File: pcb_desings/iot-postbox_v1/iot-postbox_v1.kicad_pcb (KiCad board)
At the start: 2 copper layers, 59 x 34 mm, 87 parts, among them J1 USB_B_Micro, J3 LED, J4 BAT, J5 3V3_LDO2, J6 EXT1, J7 EXT2, Q1 AO3401A, SW1 SW1, SW2 SW2, U1 ESP32-S2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

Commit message: Added iot-postbox_v1 sch to v1.1. Added minor documentation
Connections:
- net 3V3_LDO2_EN renamed LDO2_EN
- net Net-(R3-Pad1) renamed GPIO18
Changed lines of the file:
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@@
   (net 35 "Net-(JP5-Pad1)")
   (net 36 "VBAT_STAT_SENSE")
-  (net 37 "3V3_LDO2_EN")
+  (net 37 "LDO2_EN")
   (net 38 "Net-(JP6-Pad2)")
   (net 39 "/MCU/SPICS0")
@@
   (net 73 "Net-(R1-Pad1)")
   (net 74 "Net-(R2-Pad1)")
-  (net 75 "Net-(R3-Pad1)")
+  (net 75 "GPIO18")
   (footprint "Resistor_SMD:R_0805_2012Metric" locked (layer "F.Cu")
     (at 151.22 101.77 90)
@@
       (net 32 "RGB_LED_PWM") (pinfunction "GPIO17/ADC2_CH6/DAC_1") (pintype "bidirectional"))
     (pad "24" smd roundrect locked (at 1 3.4375) (size 0.22 0.875) (layers "F.Cu" "F.Paste" "F.Mask") (roundrect_rratio 0.25)
-      (net 75 "Net-(R3-Pad1)") (pinfunction "GPIO18/ADC2_CH7/DAC_2") (pintype "bidirectional"))
+      (net 75 "GPIO18") (pinfunction "GPIO18/ADC2_CH7/DAC_2") (pintype "bidirectional"))
     (pad "25" smd roundrect locked (at 1.4 3.4375) (size 0.22 0.875) (layers "F.Cu" "F.Paste" "F.Mask") (roundrect_rratio 0.25)
       (net 74 "Net-(R2-Pad1)") (pinfunction "GPIO19/ADC2_CH8/USB_D-") (pintype "bidirectional"))
@@
       (net 7 "3V3_LDO") (pinfunction "VDD3P3_RTC_IO") (pintype "power_in"))
     (pad "28" smd roundrect locked (at 2.6 3.4375) (size 0.22 0.875) (layers "F.Cu" "F.Paste" "F.Mask") (roundrect_rratio 0.25)
-      (net 37 "3V3_LDO2_EN") (pinfunction "GPIO21") (pintype "bidirectional"))
+      (net 37 "LDO2_EN") (pinfunction "GPIO21") (pintype "bidirectional"))
     (pad "29" smd roundrect locked (at 3.4375 2.6) (size 0.875 0.22) (layers "F.Cu" "F.Paste" "F.Mask") (roundrect_rratio 0.25)
       (net 40 "/MCU/SPICS1") (pinfunction "SPI_CS1/GPIO26") (pintype "bidirectional"))
@@
     (descr "Resistor SMD 0805 (2012 Metric), square (rectangular) end terminal, IPC_7351 nominal, (Body size source: IPC-SM-782 page 72, https://www.pcb-3d.com/wordpress/wp-content/uploads/ipc-sm-782a_amendment_1_and_2.pdf), generated with kicad-footprint-generator")
     (tags "resistor")
-    (property "Mouser" "RR1220P-202-D")
+    (property "Mouser" "RT0805FRE072KL")
     (property "Sheetfile" "INTERFACE.kicad_sch")
     (property "Sheetname" "INTERFACE")
@@
     (tags "resistor")
     (property "Mouser" "RC0603JR-0710KL")
+    (property "Populated" "TBD")
     (property "Sheetfile" "MCU.kicad_sch")
     (property "Sheetname" "MCU")
@@
     (fp_line (start 0.8 -0.4125) (end 0.8 0.4125) (layer "F.Fab") (width 0.1))
     (pad "1" smd roundrect locked (at -0.825 0 270) (size 0.8 0.95) (layers "F.Cu" "F.Paste" "F.Mask") (roundrect_rratio 0.25)
-      (net 75 "Net-(R3-Pad1)") (pintype "passive"))
+      (net 75 "GPIO18") (pintype "passive"))
     (pad "2" smd roundrect locked (at 0.825 0 270) (size 0.8 0.95) (layers "F.Cu" "F.Paste" "F.Mask") (roundrect_rratio 0.25)
       (net 7 "3V3_LDO") (pintype "passive"))
@@
     (descr "Inductor SMD 0402 (1005 Metric), square (rectangular) end terminal, IPC_7351 nominal, (Body size source: http://www.tortai-tech.com/upload/download/2011102023233369053.pdf), generated with kicad-footprint-generator")
     (tags "inductor")
-    (property "Mouser" "LCCI0402S4N7GTAR")
+    (property "Mouser" "LCCI0402S4N7GTAR or shielded 7447840047G")
     (property "Sheetfile" "MCU.kicad_sch")
     (property "Sheetname" "MCU")
@@
     (fp_line (start -2.3 1.25) (end -2.3 -1.25) (layer "B.CrtYd") (width 0.05))
     (pad "1" smd custom locked (at -1.3 0 270) (size 1 0.5) (layers "B.Cu" "B.Mask")
-      (net 37 "3V3_LDO2_EN") (pinfunction "A") (pintype "passive") (zone_connect 2)
+      (net 37 "LDO2_EN") (pinfunction "A") (pintype "passive") (zone_connect 2)
       (options (clearance outline) (anchor rect))
       (primitives

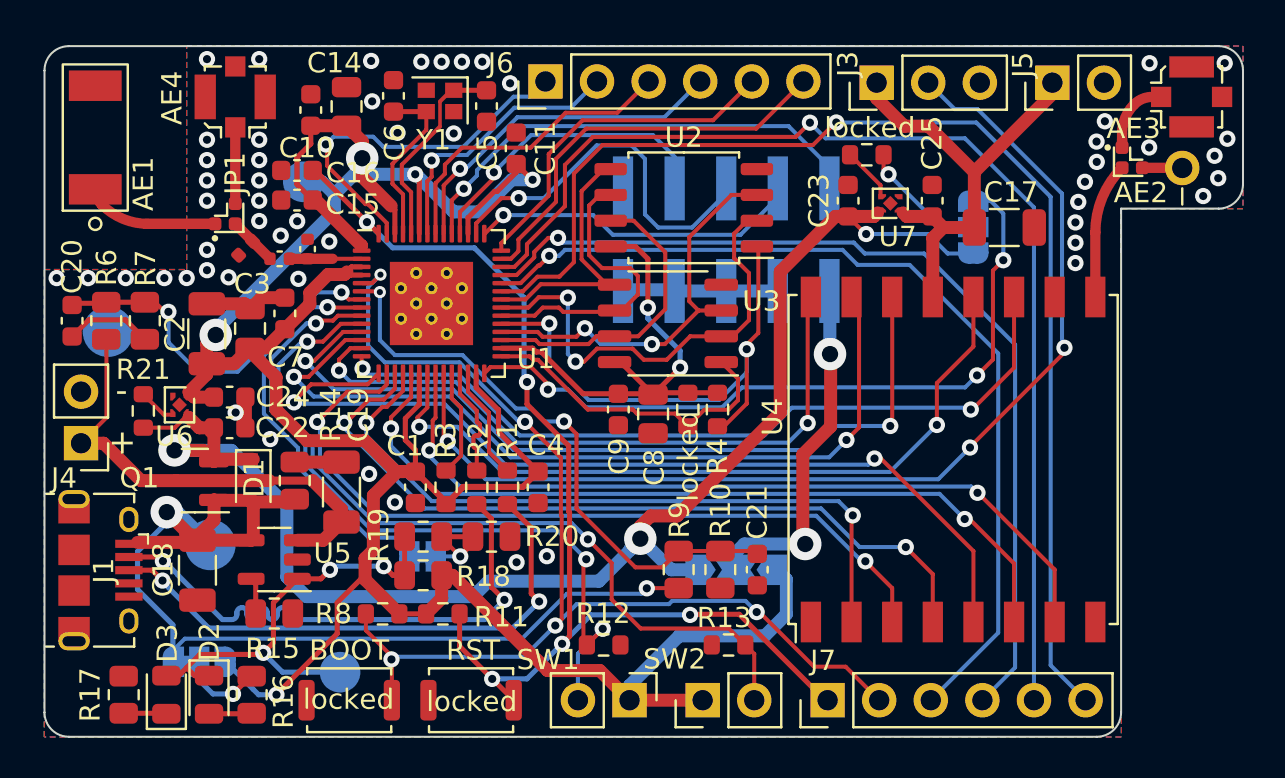
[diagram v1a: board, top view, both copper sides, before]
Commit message: Created iot-postbox v1.2 migrating to kicad v9. Fixed missing 3d designs, replaced horizontal footprints for some connectors.
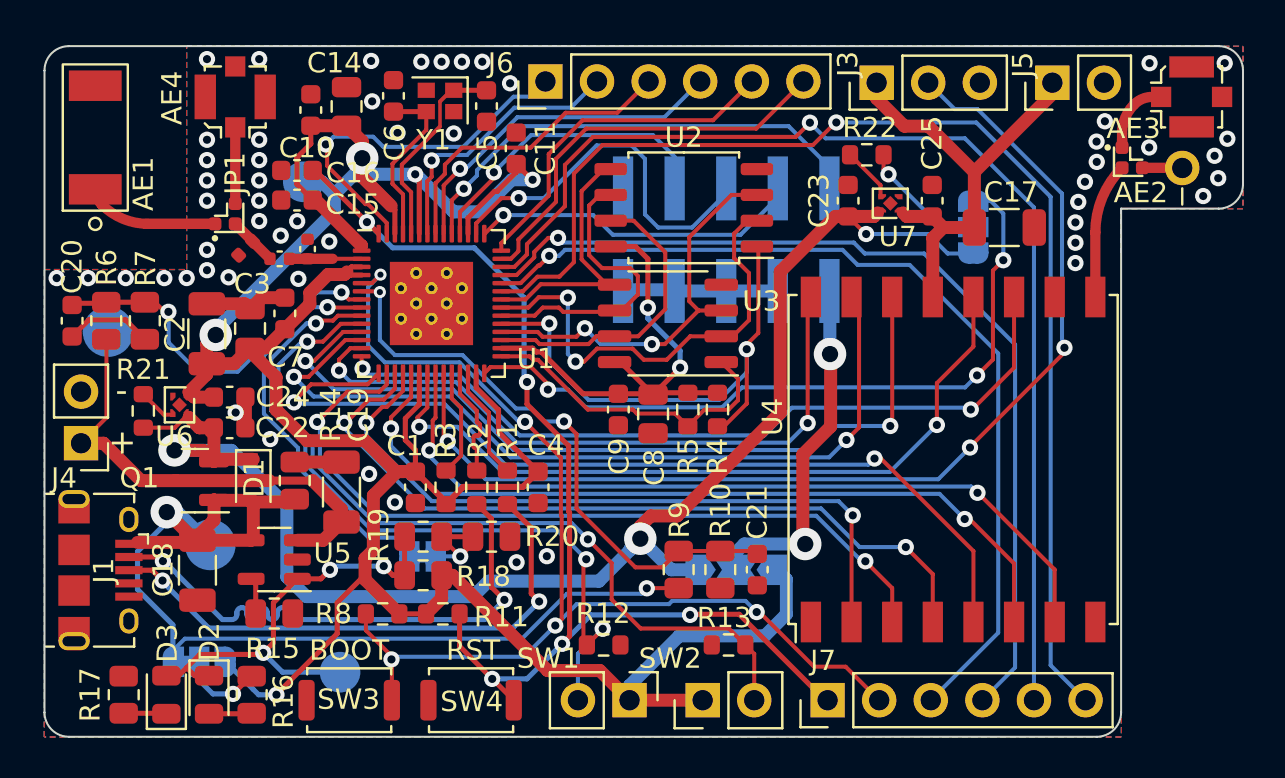
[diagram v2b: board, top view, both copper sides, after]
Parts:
- renumbered locked to J2, locked to R22, locked to R5, locked to SW3, locked to SW4
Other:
- board text added: "${COMMENT3} ${COMPANY}"
- board text removed: "${COMMENT1} ${COMPANY}"
